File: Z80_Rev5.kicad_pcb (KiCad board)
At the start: 2 copper layers, 88.5 x 64 mm, 25 parts, among them J2 UART, J3 I2C, J5 MicroSD, J7 USB_B_Mini, SW1 ON|OFF, SW2 Z80_RESET, SW3 CUSTOM, U1 Z84C00/PLCC, U3 AS6C4008-55PCN, U4 STC8H8K64U-45I-PDIP40, U5 SST39SF040

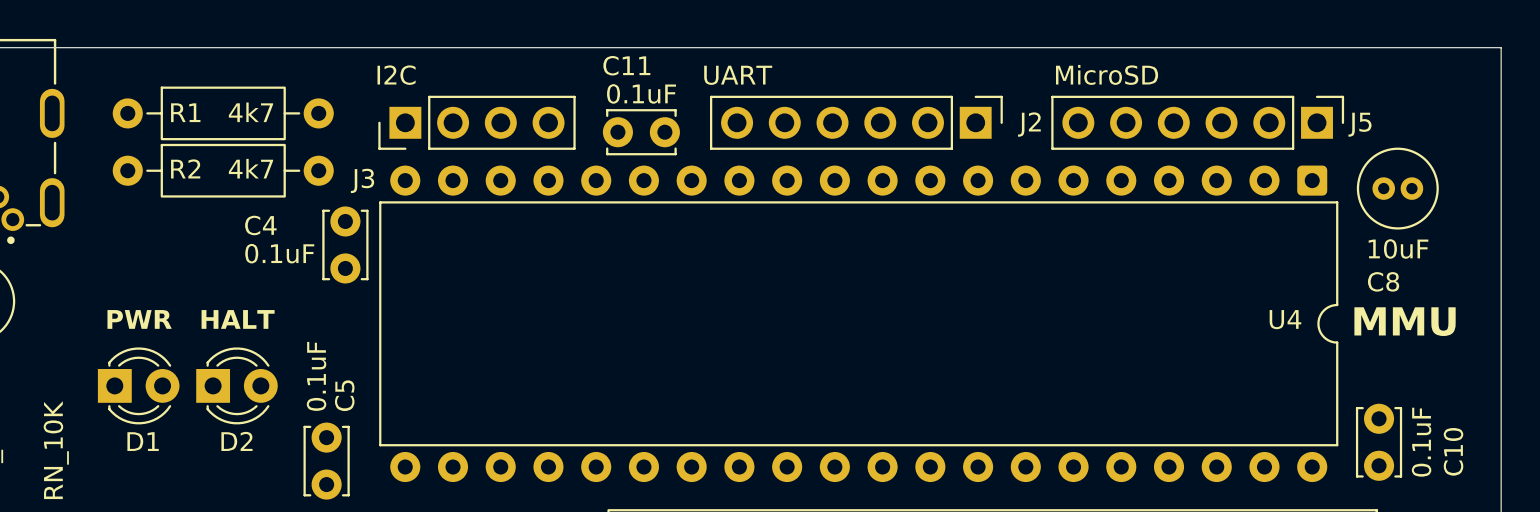
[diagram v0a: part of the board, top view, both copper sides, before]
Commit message: refine STC8 pinmap.
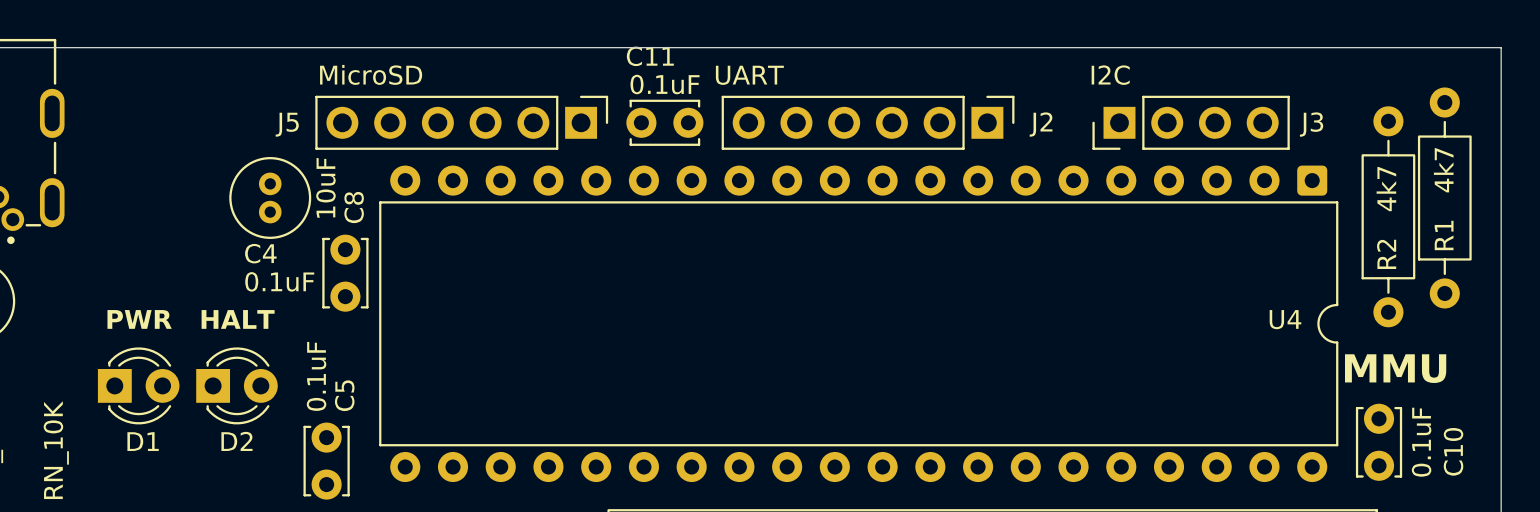
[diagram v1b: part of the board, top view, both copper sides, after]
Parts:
- moved R1 70.7 mm to (183.5, 62.6), turned to 90 degrees
- moved R2 67.5 mm to (180.5, 63.6), turned to 90 degrees
- moved C8 59.3 mm to (121.0, 58.2), turned to 90 degrees
- moved J5 39.2 mm to (137.5, 53.5)
- moved J3 38.0 mm to (166.2, 53.5)
- moved C4 1.50 mm to (125.0, 60.2)
- moved C11 1.35 mm to (140.8, 53.5)
- moved J2 0.62 mm to (159.2, 53.5)
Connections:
- U4 pad 1: /SD_CE -> /MEM_A15
- U4 pad 11: /MEM_A17 -> /MISO
- U4 pad 12: /MEM_A16 -> /SCK
- U4 pad 13: /MEM_A15 -> /Z80_CLK
- U4 pad 14: /ROM_CE -> /BUTTON
- U4 pad 15: /MEM_A18 -> /MOSI
- U4 pad 17: /RAM_CE -> /SD_CE
- U4 pad 2: /SCK -> /MEM_A16
- U4 pad 21: /IORQ -> /D-
- U4 pad 22: /RESET -> /D+
- U4 pad 23: /RD -> /IORQ
- U4 pad 25: /SDA -> /RESET
- U4 pad 26: /SCL -> /MREQ
- U4 pad 27: /MREQ -> /RD
- U4 pad 3: /MOSI -> /MEM_A17
- U4 pad 4: /MISO -> /MEM_A18
- U4 pad 5: /Z80_CLK -> /ROM_CE
- U4 pad 6: /BUTTON -> /RAM_CE
- U4 pad 7: /D+ -> /SDA
- U4 pad 8: /D- -> /SCL
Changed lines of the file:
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@@
 	(footprint "Connector_PinHeader_2.54mm:PinHeader_1x04_P2.54mm_Vertical"
 		(layer "F.Cu")
-		(at 128.19 53.5 90)
+		(at 166.19 53.5 90)
 		(descr "Through hole straight pin header, 1x04, 2.54mm pitch, single row")
 		(tags "Through hole pin header THT 1x04 2.54mm single row")
 		(property "Reference" "J3"
-			(at -3 -2.19 180)
+			(at 0 10.31 180)
 			(layer "F.SilkS")
 			(effects
@@
 	(footprint "Capacitor_THT:C_Disc_D3.4mm_W2.1mm_P2.50mm"
 		(layer "F.Cu")
-		(at 125 58.75 -90)
+		(at 125 60.25 -90)
 		(descr "C, Disc series, Radial, pin pitch=2.50mm, diameter*width=3.4*2.1mm^2, Capacitor, http://www.vishay.com/docs/45233/krseries.pdf")
 		(tags "C Disc series Radial pin pitch 2.50mm diameter 3.4mm width 2.1mm Capacitor")
@@
 	(footprint "Capacitor_THT:C_Radial_D4.0mm_H5.0mm_P1.50mm"
 		(layer "F.Cu")
-		(at 180.25 57)
+		(at 121 58.25 90)
 		(descr "C, Radial series, Radial, pin pitch=1.50mm, diameter=4mm, height=5mm, Non-Polar Electrolytic Capacitor")
 		(tags "C Radial series Radial pin pitch 1.50mm diameter 4mm height 5mm Non-Polar Electrolytic Capacitor")
 		(property "Reference" "C8"
-			(at 0 5 0)
+			(at 0.25 4.5 90)
 			(layer "F.SilkS")
 			(effects
@@
 		)
 		(property "Value" "10uF"
-			(at 0.75 3.25 0)
+			(at 1.25 3 90)
 			(layer "F.SilkS")
 			(effects
@@
 		)
 		(property "Datasheet" ""
-			(at 0 0 0)
+			(at 0 0 90)
 			(layer "F.Fab")
 			(hide yes)
@@
 		)
 		(property "Description" "Unpolarized capacitor"
-			(at 0 0 0)
+			(at 0 0 90)
 			(layer "F.Fab")
 			(hide yes)
@@
 		)
 		(fp_text user "${REFERENCE}"
-			(at 0.75 0 0)
+			(at 0.75 0 90)
 			(layer "F.Fab")
 			(effects
@@
 		)
 		(pad "1" thru_hole circle
-			(at 0 0)
+			(at 0 0 90)
 			(size 1.2 1.2)
 			(drill 0.6)
@@
 		)
 		(pad "2" thru_hole circle
-			(at 1.5 0)
+			(at 1.5 0 90)
 			(size 1.2 1.2)
 			(drill 0.6)
@@
 	(footprint "Connector_PinHeader_2.54mm:PinHeader_1x06_P2.54mm_Vertical"
 		(layer "F.Cu")
-		(at 158.54 53.5 -90)
+		(at 159.16 53.5 -90)
 		(descr "Through hole straight pin header, 1x06, 2.54mm pitch, single row")
 		(tags "Through hole pin header THT 1x06 2.54mm single row")
@@
 	(footprint "Resistor_THT:R_Axial_DIN0207_L6.3mm_D2.5mm_P10.16mm_Horizontal"
 		(layer "F.Cu")
-		(at 113.42 56.05)
+		(at 180.5 63.58 90)
 		(descr "Resistor, Axial_DIN0207 series, Axial, Horizontal, pin pitch=10.16mm, 0.25W = 1/4W, length*diameter=6.3*2.5mm^2, http://cdn-reichelt.de/documents/datenblatt/B400/1_4W%23YAG.pdf")
 		(tags "Resistor Axial_DIN0207 series Axial Horizontal pin pitch 10.16mm 0.25W = 1/4W length 6.3mm diameter 2.5mm")
 		(property "Reference" "R2"
-			(at 3.08 -0.05 0)
+			(at 3.08 -0.05 90)
 			(layer "F.SilkS")
 			(effects
@@
 		)
 		(property "Value" "4k7"
-			(at 6.58 -0.05 0)
+			(at 6.58 -0.05 90)
 			(layer "F.SilkS")
 			(effects
@@
 		)
 		(property "Datasheet" ""
-			(at 0 0 0)
+			(at 0 0 90)
 			(layer "F.Fab")
 			(hide yes)
@@
 		)
 		(property "Description" "Resistor"
-			(at 0 0 0)
+			(at 0 0 90)
 			(layer "F.Fab")
 			(hide yes)
@@
 		(duplicate_pad_numbers_are_jumpers no)
 		(fp_line
-			(start 1.04 0)
-			(end 1.81 0)
+			(start 9.12 0)
+			(end 8.35 0)
 			(stroke
 				(width 0.12)
@@
 		)
 		(fp_line
-			(start 9.12 0)
-			(end 8.35 0)
+			(start 1.04 0)
+			(end 1.81 0)
 			(stroke
 				(width 0.12)
@@
 		)
 		(fp_line
-			(start 0 0)
-			(end 1.93 0)
+			(start 10.16 0)
+			(end 8.23 0)
 			(stroke
 				(width 0.1)
@@
 		)
 		(fp_line
-			(start 10.16 0)
-			(end 8.23 0)
+			(start 0 0)
+			(end 1.93 0)
 			(stroke
 				(width 0.1)
@@
 		)
 		(fp_text user "${REFERENCE}"
-			(at 3.08 -0.05 0)
+			(at 3.08 -0.05 90)
 			(layer "F.Fab")
 			(effects
@@
 		)
 		(pad "1" thru_hole circle
-			(at 0 0)
+			(at 0 0 90)
 			(size 1.6 1.6)
 			(drill 0.8)
@@
 		)
 		(pad "2" thru_hole circle
-			(at 10.16 0)
+			(at 10.16 0 90)
 			(size 1.6 1.6)
 			(drill 0.8)
@@
 			(remove_unused_layers no)
 			(roundrect_rratio 0.15625)
-			(net "/SD_CE")
+			(net "/MEM_A15")
 			(pinfunction "P0.0_1")
 			(pintype "bidirectional")
@@
 			(layers "*.Cu" "*.Mask")
 			(remove_unused_layers no)
-			(net "/SCK")
+			(net "/MEM_A16")
 			(pinfunction "P0.1_2")
 			(pintype "bidirectional")
@@
 			(layers "*.Cu" "*.Mask")
 			(remove_unused_layers no)
-			(net "/MOSI")
+			(net "/MEM_A17")
 			(pinfunction "P0.2_3")
 			(pintype "bidirectional")
@@
 			(layers "*.Cu" "*.Mask")
 			(remove_unused_layers no)
-			(net "/MISO")
+			(net "/MEM_A18")
 			(pinfunction "P0.3_4")
 			(pintype "bidirectional")
@@
 			(layers "*.Cu" "*.Mask")
 			(remove_unused_layers no)
-			(net "/Z80_CLK")
+			(net "/ROM_CE")
 			(pinfunction "P0.4_5")
 			(pintype "bidirectional")
@@
 			(layers "*.Cu" "*.Mask")
 			(remove_unused_layers no)
-			(net "/BUTTON")
+			(net "/RAM_CE")
 			(pinfunction "P0.5_6")
 			(pintype "bidirectional")
@@
 			(layers "*.Cu" "*.Mask")
 			(remove_unused_layers no)
-			(net "/D+")
+			(net "/SDA")
 			(pinfunction "P0.6_7")
 			(pintype "bidirectional")
@@
 			(layers "*.Cu" "*.Mask")
 			(remove_unused_layers no)
-			(net "/D-")
+			(net "/SCL")
 			(pinfunction "P0.7_8")
 			(pintype "bidirectional")
@@
 			(layers "*.Cu" "*.Mask")
 			(remove_unused_layers no)
-			(net "/MEM_A17")
+			(net "/MISO")
 			(pinfunction "P1.4_11")
 			(pintype "bidirectional")
@@
 			(layers "*.Cu" "*.Mask")
 			(remove_unused_layers no)
-			(net "/MEM_A16")
+			(net "/SCK")
 			(pinfunction "P1.5_12")
 			(pintype "bidirectional")
@@
 			(layers "*.Cu" "*.Mask")
 			(remove_unused_layers no)
-			(net "/MEM_A15")
+			(net "/Z80_CLK")
 			(pinfunction "P1.6_13")
 			(pintype "bidirectional")
@@
 			(layers "*.Cu" "*.Mask")
 			(remove_unused_layers no)
-			(net "/ROM_CE")
+			(net "/BUTTON")
 			(pinfunction "P1.7_14")
 			(pintype "bidirectional")
@@
 			(layers "*.Cu" "*.Mask")
 			(remove_unused_layers no)
-			(net "/MEM_A18")
+			(net "/MOSI")
 			(pinfunction "P1.3_15")
 			(pintype "bidirectional")
@@
 			(layers "*.Cu" "*.Mask")
 			(remove_unused_layers no)
-			(net "/RAM_CE")
+			(net "/SD_CE")
 			(pinfunction "P5.4_17")
 			(pintype "bidirectional")
@@
 			(layers "*.Cu" "*.Mask")
 			(remove_unused_layers no)
-			(net "/IORQ")
+			(net "/D-")
 			(pinfunction "P3.0_21")
 			(pintype "bidirectional")
@@
 			(layers "*.Cu" "*.Mask")
 			(remove_unused_layers no)
-			(net "/RESET")
+			(net "/D+")
 			(pinfunction "P3.1_22")
 			(pintype "bidirectional")
@@
 			(layers "*.Cu" "*.Mask")
 			(remove_unused_layers no)
-			(net "/RD")
+			(net "/IORQ")
 			(pinfunction "P3.2_23")
 			(pintype "bidirectional")
@@
 			(layers "*.Cu" "*.Mask")
 			(remove_unused_layers no)
-			(net "/SDA")
+			(net "/RESET")
 			(pinfunction "P3.4_25")
 			(pintype "bidirectional")
@@
 			(layers "*.Cu" "*.Mask")
 			(remove_unused_layers no)
-			(net "/SCL")
+			(net "/MREQ")
 			(pinfunction "P3.5_26")
 			(pintype "bidirectional")
@@
 			(layers "*.Cu" "*.Mask")
 			(remove_unused_layers no)
-			(net "/MREQ")
+			(net "/RD")
 			(pinfunction "P3.6_27")
 			(pintype "bidirectional")
@@
 	(footprint "Capacitor_THT:C_Disc_D3.4mm_W2.1mm_P2.50mm"
 		(layer "F.Cu")
-		(at 139.5 54)
+		(at 140.75 53.5)
 		(descr "C, Disc series, Radial, pin pitch=2.50mm, diameter*width=3.4*2.1mm^2, Capacitor, http://www.vishay.com/docs/45233/krseries.pdf")
 		(tags "C Disc series Radial pin pitch 2.50mm diameter 3.4mm width 2.1mm Capacitor")
@@
 	(footprint "Resistor_THT:R_Axial_DIN0207_L6.3mm_D2.5mm_P10.16mm_Horizontal"
 		(layer "F.Cu")
-		(at 113.42 53)
+		(at 183.5 62.58 90)
 		(descr "Resistor, Axial_DIN0207 series, Axial, Horizontal, pin pitch=10.16mm, 0.25W = 1/4W, length*diameter=6.3*2.5mm^2, http://cdn-reichelt.de/documents/datenblatt/B400/1_4W%23YAG.pdf")
 		(tags "Resistor Axial_DIN0207 series Axial Horizontal pin pitch 10.16mm 0.25W = 1/4W length 6.3mm diameter 2.5mm")
 		(property "Reference" "R1"
-			(at 3.08 0 0)
+			(at 3.08 0 90)
 			(layer "F.SilkS")
 			(effects
@@
 		)
 		(property "Value" "4k7"
-			(at 6.58 0 0)
+			(at 6.58 0 90)
 			(layer "F.SilkS")
 			(effects
@@
 		)
 		(property "Datasheet" ""
-			(at 0 0 0)
+			(at 0 0 90)
 			(layer "F.Fab")
 			(hide yes)
@@
 		)
 		(property "Description" "Resistor"
-			(at 0 0 0)
+			(at 0 0 90)
 			(layer "F.Fab")
 			(hide yes)
@@
 		(duplicate_pad_numbers_are_jumpers no)
 		(fp_line
-			(start 1.04 0)
-			(end 1.81 0)
+			(start 9.12 0)
+			(end 8.35 0)
 			(stroke
 				(width 0.12)
@@
 		)
 		(fp_line
-			(start 9.12 0)
-			(end 8.35 0)
+			(start 1.04 0)
+			(end 1.81 0)
 			(stroke
 				(width 0.12)
@@
 		)
 		(fp_line
-			(start 0 0)
-			(end 1.93 0)
+			(start 10.16 0)
+			(end 8.23 0)
 			(stroke
 				(width 0.1)
@@
 		)
 		(fp_line
-			(start 10.16 0)
-			(end 8.23 0)
+			(start 0 0)
+			(end 1.93 0)
 			(stroke
 				(width 0.1)
@@
 		)
 		(fp_text user "${REFERENCE}"
-			(at 3.08 0 0)
+			(at 3.08 0 90)
 			(layer "F.Fab")
 			(effects
@@
 		)
 		(pad "1" thru_hole circle
-			(at 0 0)
+			(at 0 0 90)
 			(size 1.6 1.6)
 			(drill 0.8)
@@
 		)
 		(pad "2" thru_hole circle
-			(at 10.16 0)
+			(at 10.16 0 90)
 			(size 1.6 1.6)
 			(drill 0.8)
@@
 	(footprint "Connector_PinHeader_2.54mm:PinHeader_1x06_P2.54mm_Vertical"
 		(layer "F.Cu")
-		(at 176.7 53.5 -90)
+		(at 137.54 53.5 -90)
 		(descr "Through hole straight pin header, 1x06, 2.54mm pitch, single row")
 		(tags "Through hole pin header THT 1x06 2.54mm single row")
 		(property "Reference" "J5"
-			(at 0 -2.38 180)
+			(at 0 15.54 180)
 			(layer "F.SilkS")
 			(effects
@@
 	)
 	(gr_text "MMU"
-		(at 178.5 65 0)
+		(at 178 67.5 0)
 		(layer "F.SilkS" knockout)
 		(effects
